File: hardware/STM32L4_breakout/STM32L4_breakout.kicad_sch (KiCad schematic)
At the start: 49 parts

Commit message: breakout board schematic WIP
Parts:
- removed R?: 1K, symbol Device:R_Small_US
- added C? (x2): 1uF, symbol Device:C_Small
- added C? (x4): 10uF, symbol Device:C_Small
- added C? (x2): 100nF, symbol Device:C_Small
- added C?: 10nF, symbol Device:C_Small
- added J?: UART4, symbol Connector_Generic:Conn_01x03
- added R?: 0 - DNI, symbol Device:R_US
- added R?: 0, symbol Device:R_US
- added U?: LD3985M33R_SOT23, Package_TO_SOT_SMD:SOT-23-5, symbol Regulator_Linear:LD3985M33R_SOT23
- C?: value 10u -> 10uF
- R? (x4): value 10k -> 2k2
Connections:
- net +12V: now also C?.1
- net +3.3V: now also C?.1, R?.1
- net +5V: now also C?.1, C?.1, C?.1, C?.1, R?.1, U?.1 (VIN), U?.3 (INH); no longer R?.1, R?.1, R?.1, R?.1
- net CARDCS_5V: now also J?.5 (Pin_5)
- net D7: now also J?.8 (Pin_8)
- net GND: now also C?.2, C?.2, C?.2, C?.2, C?.2, C?.2, C?.2, C?.2, C?.2, J?.3 (Pin_3), U?.2 (GND)
- net LEDK: now also J?.4 (Pin_4)
- net RELAY1_CTRL: now also J?.7 (Pin_7)
- net RELAY2_CTRL: now also J?.6 (Pin_6)
- net RT_CS: now also J?.1 (Pin_1)
- net SPI1_MISO: now also J?.5 (Pin_5)
- net SPI1_MOSI: now also J?.4 (Pin_4)
- net SPI1_SCK: now also J?.6 (Pin_6)
- net TFT_CS: now also J?.3 (Pin_3)
- net TFT_DC: now also J?.2 (Pin_2)
- net UART4_TX: now reaches J?.1 (Pin_1)
- net UART4_TX: now also U?.14 (PA0), J?.1 (Pin_1)
- net UART4_RX: now reaches J?.2 (Pin_2)
- net UART4_RX: now also U?.15 (PA1), J?.2 (Pin_2)
- net I2C3_SCL: now reaches U?.8 (PC0)
- net I2C3_SDA: now reaches U?.9 (PC1)
- net VMEM: now reaches J?.1 (Pin_1)
- net VMEM: now also C?.1, C?.1, U?.5 (VOUT)
- new net: R?.1, R?.1, R?.1, R?.1, R?.2, R?.2
- new net: C?.1, U?.4 (BYP)
- no-connect marks 33 -> 30
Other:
- moved on the sheet: C?, J?, R?, U?

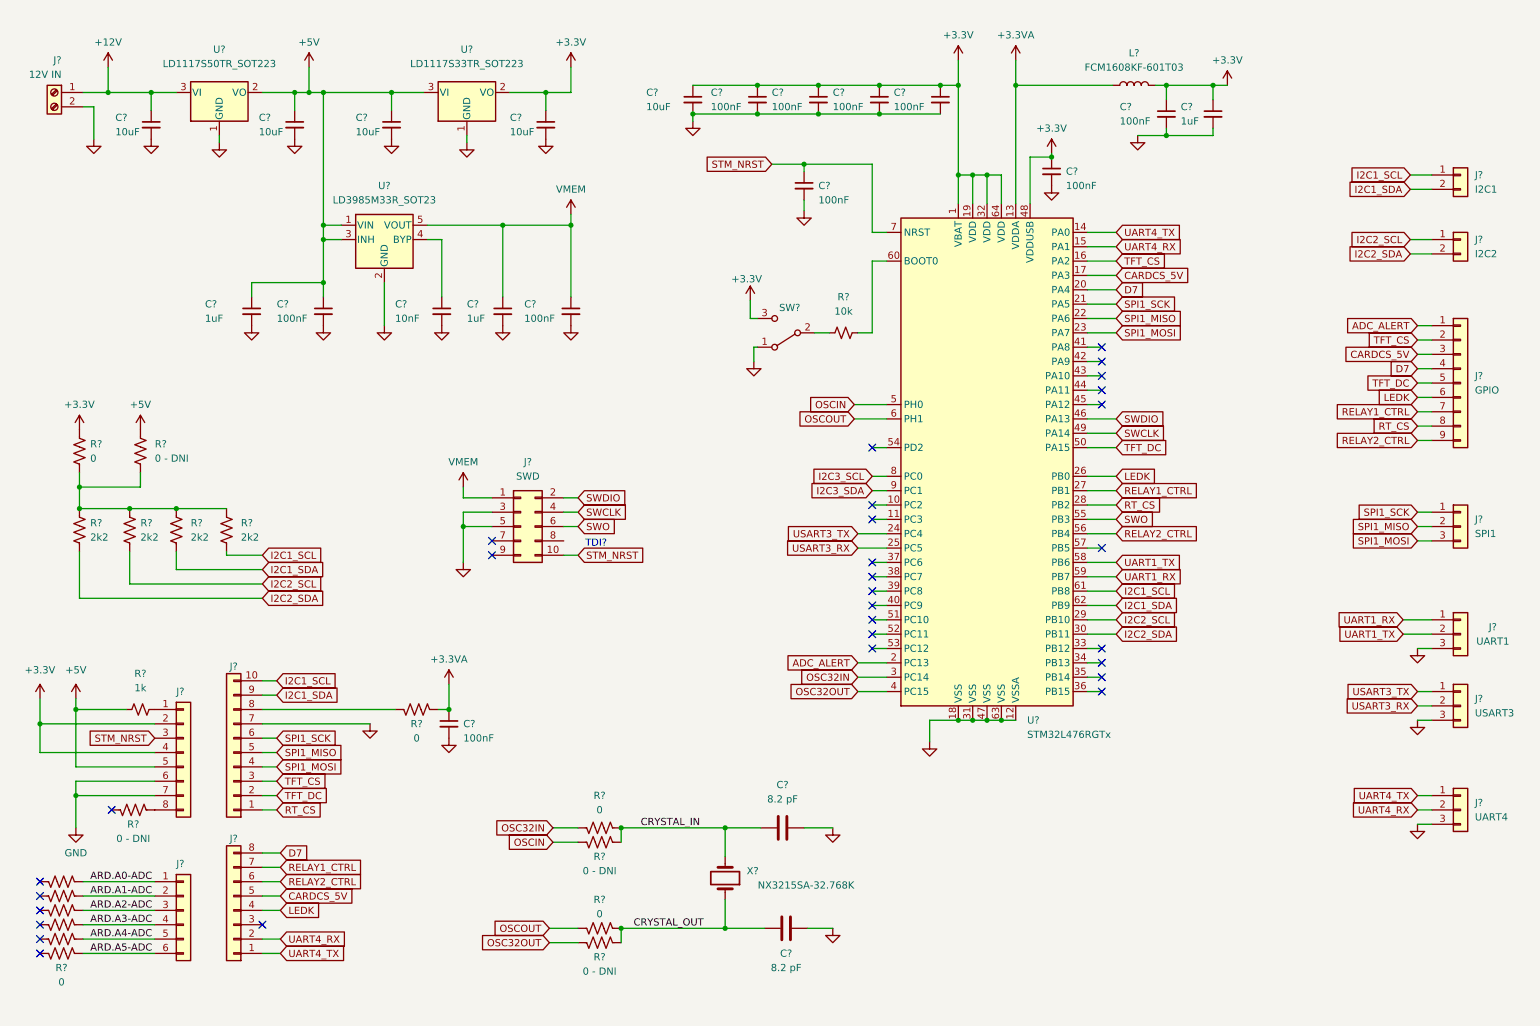
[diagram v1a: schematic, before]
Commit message: Update STM32L4_breakout.kicad_sch
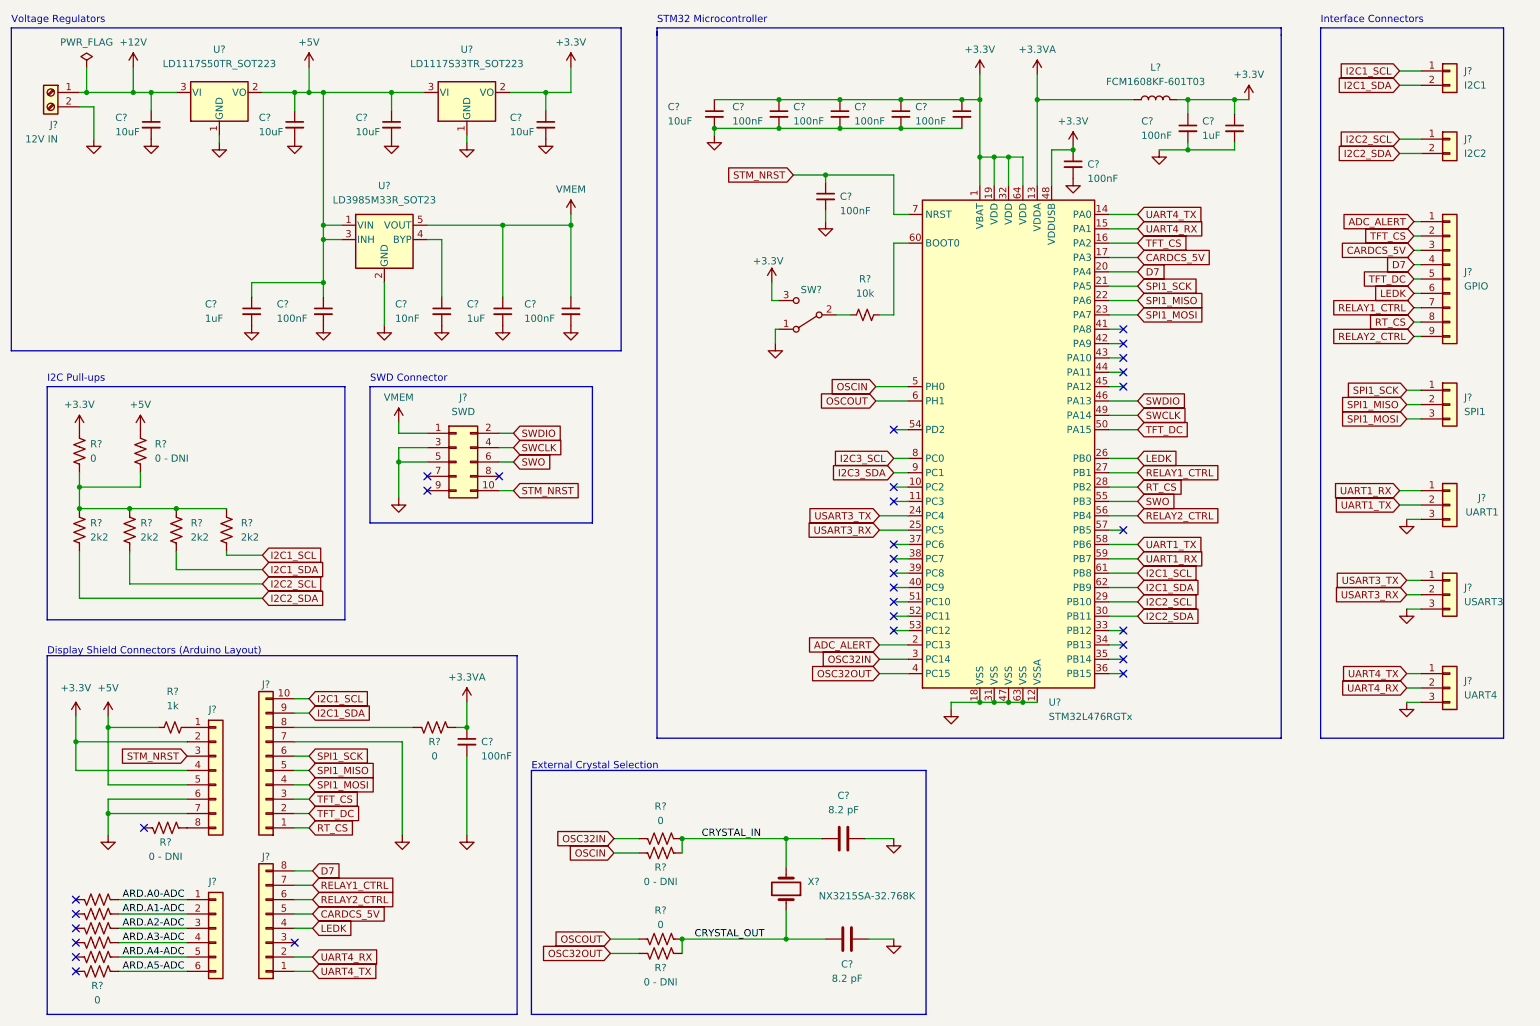
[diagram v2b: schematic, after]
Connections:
- no-connect marks 30 -> 31
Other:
- note added: "Display Shield Connectors (Arduino Layout)"
- note added: "External Crystal Selection"
- note added: "I2C Pull-ups"
- note added: "Interface Connectors"
- note added: "STM32 Microcontroller"
- note added: "SWD Connector"
- note added: "Voltage Regulators"
- note removed: "TDI?"
- moved on the sheet: C?, J?, L?, R?, SW?, U?, X?

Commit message: annotated breakout board schematic
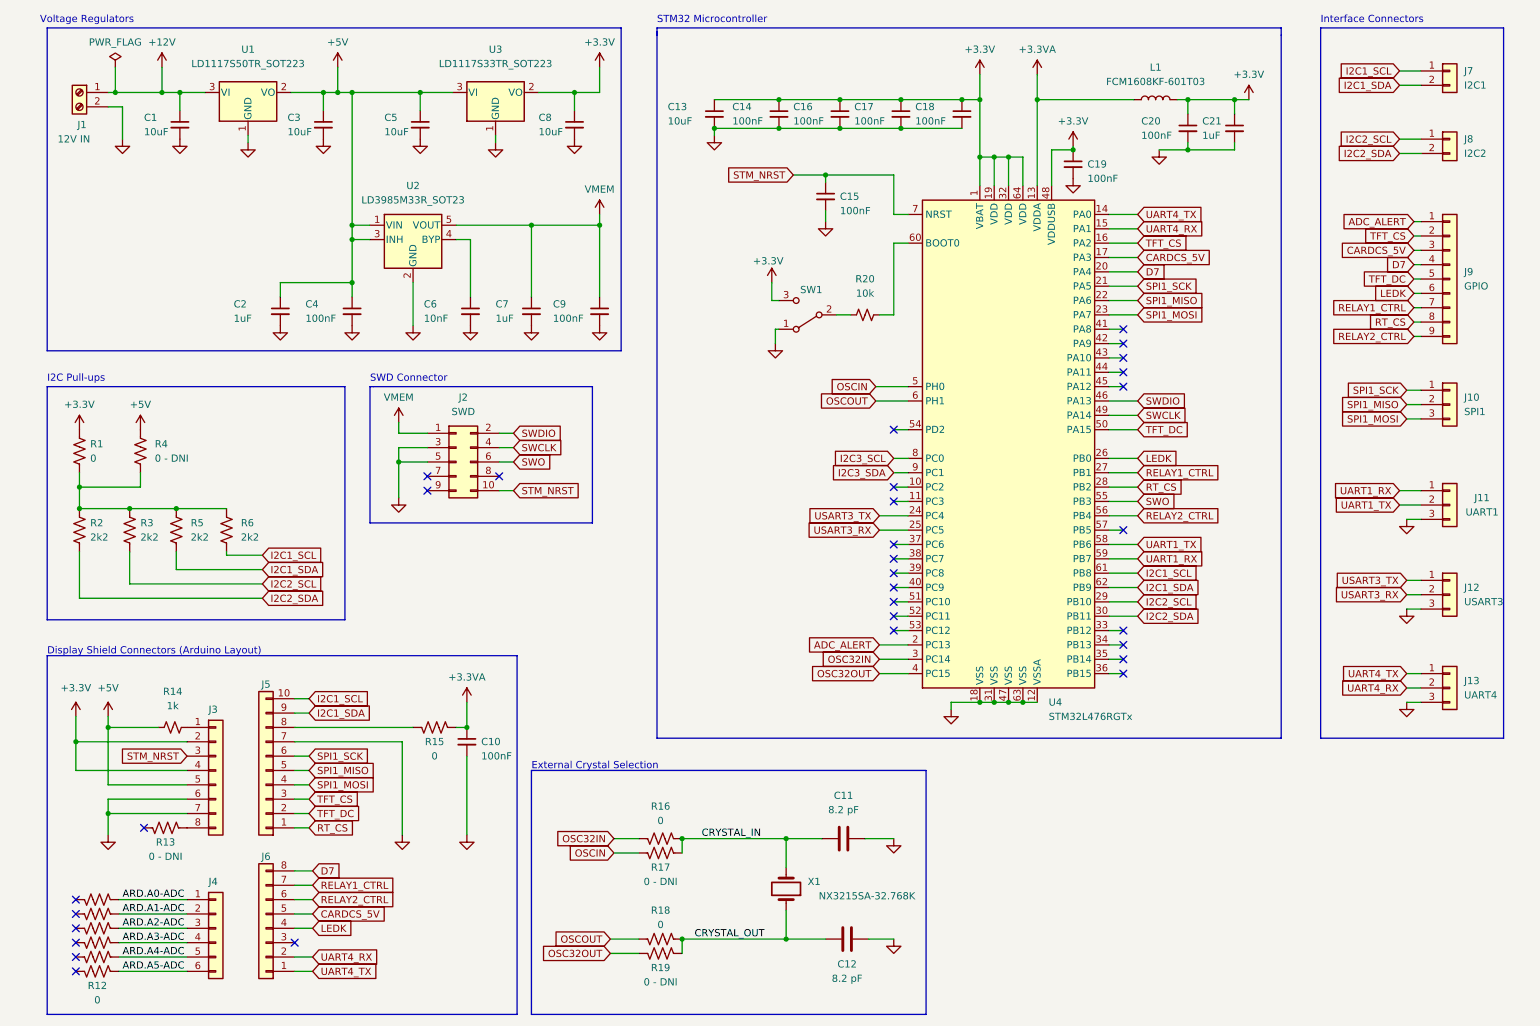
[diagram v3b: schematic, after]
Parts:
- gave numbers to parts that had none: 61
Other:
- moved on the sheet: C1, C2, C3, C4, C5, C6, C7, C8, C9, J1, U1, U2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

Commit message: breakout schematic passes ERC
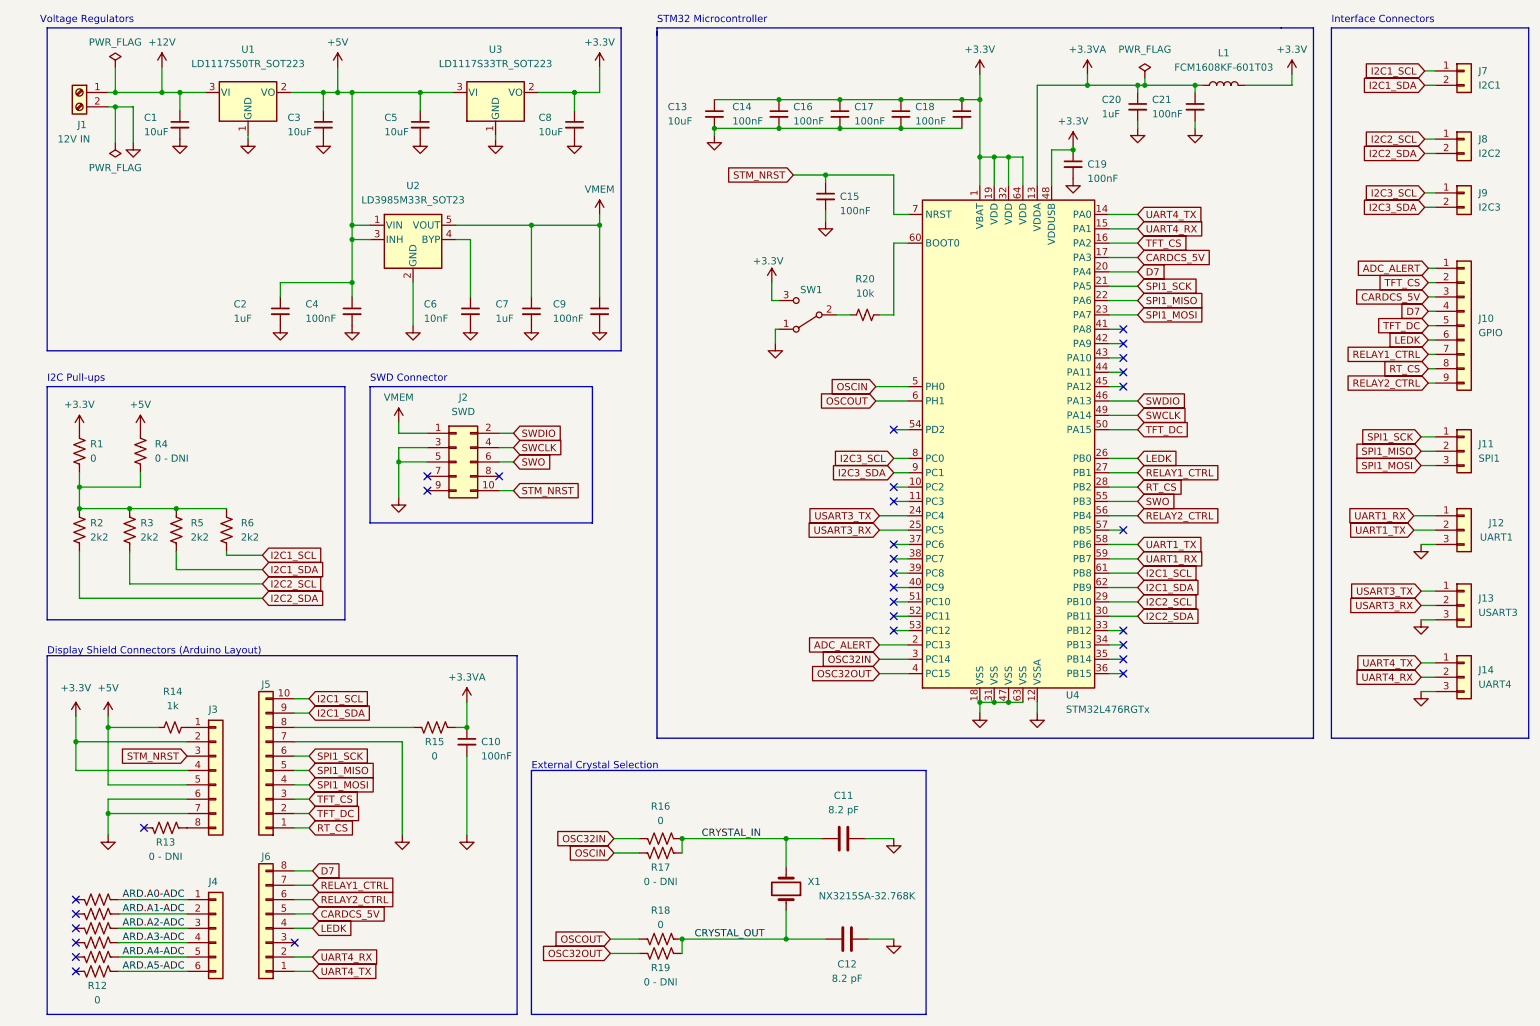
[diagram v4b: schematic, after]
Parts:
- added J9: I2C3, symbol Connector_Generic:Conn_01x02
- C20: value 100nF -> 1uF
- C21: value 1uF -> 100nF
- renumbered J9 to J10, J10 to J11, J11 to J12, J12 to J13, J13 to J14
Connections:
- net +3.3V: no longer C20.1, C21.1
- net +3.3VA: now also C20.1, C21.1
- net I2C3_SCL: now also J9.1 (Pin_1)
- net I2C3_SDA: now also J9.2 (Pin_2)
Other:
- moved on the sheet: C20, C21, J10, J11, J12, J13, J14, J7, J8, L1

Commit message: breakout schematic review WIP
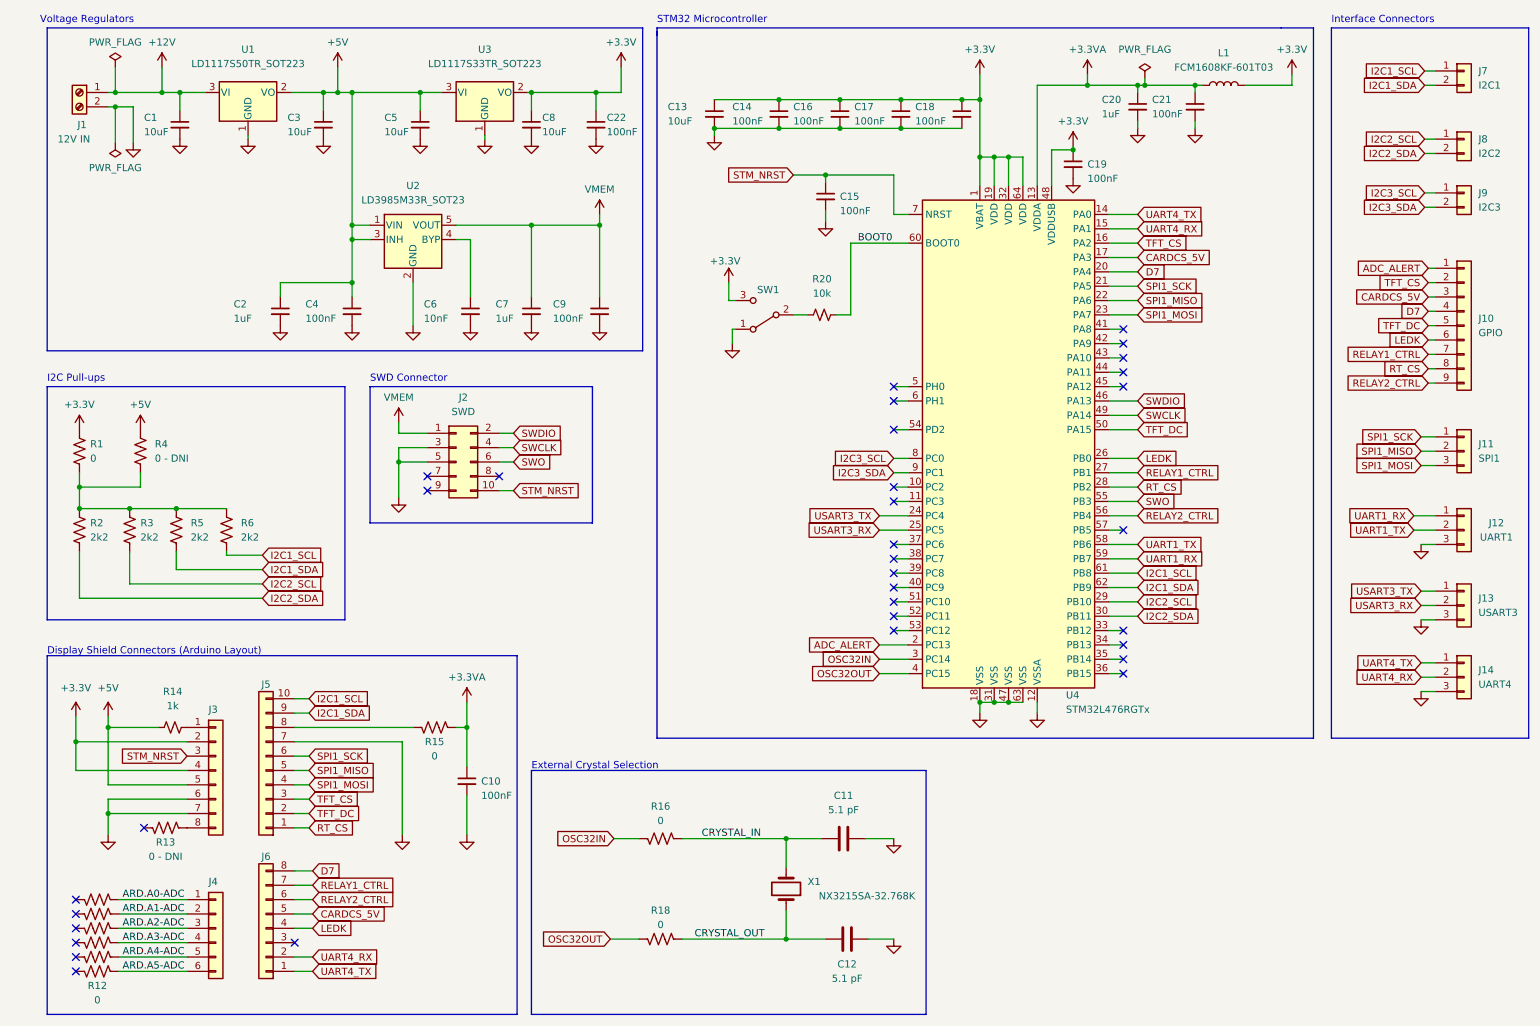
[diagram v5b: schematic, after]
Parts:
- removed R17, R19: 0 - DNI, symbol Device:R_US
- added C22: 100nF, symbol Device:C_Small
- C11, C12: value 8.2 pF -> 5.1 pF
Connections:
- net +3.3V: now also C22.1
- net GND: now also C22.2
- net OSC32OUT: now also R18.2
- net BOOT0: now reaches R20.2, U4.60 (BOOT0)
- net OSCIN: no longer names the net of U4.5 (PH0)
- net OSCOUT: no longer names the net of U4.6 (PH1)
- net OSCOUT: no longer R18.2
- no-connect marks 31 -> 33
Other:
- moved on the sheet: C10, C8, R20, SW1, U3

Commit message: breakout board schematic review complete
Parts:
- added J15: 3.3V, symbol Connector_Generic:Conn_01x02
- added J16: 5V, symbol Connector_Generic:Conn_01x02
- added J17: 12V, symbol Connector_Generic:Conn_01x02
- C13: value 10uF -> 100nF
- J12: value UART1 -> USART1
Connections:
- net +12V: now also J17.1 (Pin_1), J17.2 (Pin_2)
- net +3.3V: now also J15.1 (Pin_1), J15.2 (Pin_2)
- net +5V: now also J16.1 (Pin_1), J16.2 (Pin_2)
- net UART1_RX renamed USART1_RX
- net UART1_TX renamed USART1_TX
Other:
- moved on the sheet: J11, J12, J13, J14

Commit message: selected packages
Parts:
- C1, C2, C20, C3, C5, C7, C8: footprint (none) -> Capacitor_SMD:C_0805_2012Metric
- C10, C11, C12, C13, C14, C15, C16, C17, C18, C19, C21, C22, C4, C6, C9: footprint (none) -> Capacitor_SMD:C_0603_1608Metric
- J1: footprint (none) -> TerminalBlock_Phoenix:TerminalBlock_Phoenix_MKDS-1,5-2_1x02_P5.00mm_Horizontal
- J10: footprint (none) -> Connector_PinHeader_2.54mm:PinHeader_1x09_P2.54mm_Vertical
- J11, J12, J13, J14: footprint (none) -> Connector_PinHeader_2.54mm:PinHeader_1x03_P2.54mm_Vertical
- J15, J16, J17, J7, J8, J9: footprint (none) -> Connector_PinHeader_2.54mm:PinHeader_1x02_P2.54mm_Vertical
- J2: footprint (none) -> Connector_PinHeader_2.54mm:PinHeader_2x05_P2.54mm_Vertical
- J3, J6: footprint (none) -> Connector_PinHeader_2.54mm:PinHeader_1x08_P2.54mm_Vertical
- J4: footprint (none) -> Connector_PinHeader_2.54mm:PinHeader_1x06_P2.54mm_Vertical
- J5: footprint (none) -> Connector_PinHeader_2.54mm:PinHeader_1x10_P2.54mm_Vertical
- L1: footprint (none) -> Inductor_SMD:L_0603_1608Metric
- R1, R10, R11, R12, R13, R14, R15, R16, R18, R2, R20, R3, R4, R5, R6, R7, R8, R9: footprint (none) -> Resistor_SMD:R_0603_1608Metric
- SW1: footprint (none) -> Button_Switch_SMD:SW_SPDT_CK-JS102011SAQN
- X1: footprint (none) -> Crystal:Crystal_SMD_3215-2Pin_3.2x1.5mm

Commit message: breakout board PCB layout WIP
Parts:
- R15: value 0 -> 0R
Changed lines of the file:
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@@
     (in_bom no) (on_board yes)
     (property "Reference" "R15" (id 0) (at 87.63 145.415 90))
-    (property "Value" "0 " (id 1) (at 87.63 147.955 90))
+    (property "Value" "0R" (id 1) (at 87.63 147.955 90))
     (property "Footprint" "Resistor_SMD:R_0603_1608Metric" (id 2) (at 87.376 141.859 90)
       (effects (font (size 1.27 1.27)) hide)
@@
     )
     (path "/2db0bf93-9d75-460a-9d07-54f6be7ef140"
-      (reference "R15") (unit 1) (value "0 ") (footprint "Resistor_SMD:R_0603_1608Metric")
+      (reference "R15") (unit 1) (value "0R") (footprint "Resistor_SMD:R_0603_1608Metric")
     )
     (path "/c8ca5e13-ce47-47fc-bf42-0c1386fc6746"
